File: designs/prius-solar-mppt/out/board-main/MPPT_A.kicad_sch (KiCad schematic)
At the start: 79 parts, among them J101 1757242, Q101 IAUC100N10, Q102 MMBTA42, Q103 IAUC100N10, Q104 IAUC100N10, Q105 IAUC100N10, Q106 IAUC100N10, U101 LM74700-Q1, U102 INA186A2QDBVRQ1, U103 LM5176QPWPRQ1, U104 TLV9001-Q1

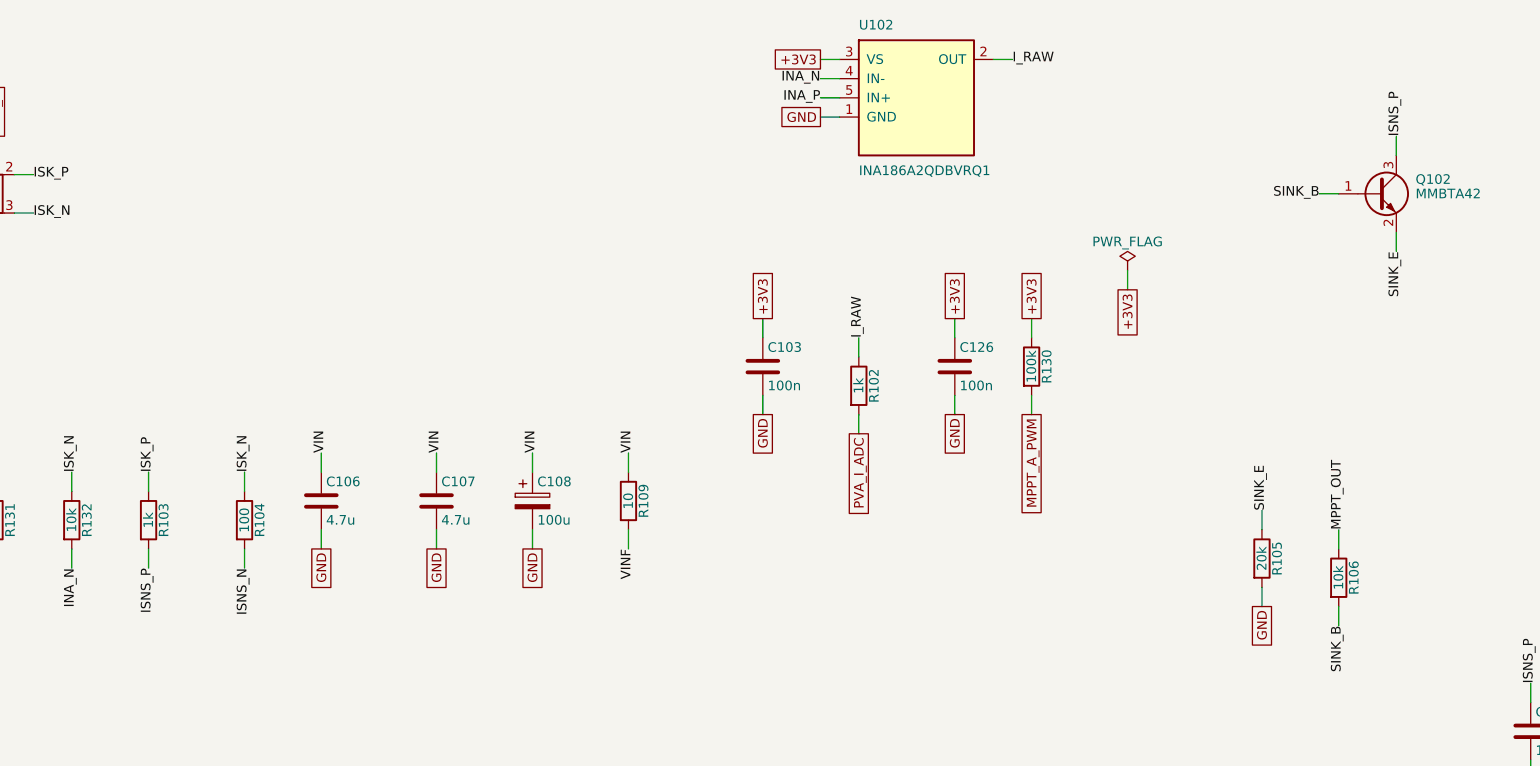
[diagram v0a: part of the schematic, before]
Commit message: designs/prius-solar-mppt: rework for the 2017 Prius Prime (Li-ion), charging car on and off
User decisions (2026-10-23): it is a Prius Prime with the Li-ion pack; it must charge
with the car on or off, be smart, and be weak enough that the pack cannot get into
trouble (stop by 80 %, voltage clamp, temperature compensation).

- Pack: 95 cells in series; no Prius pack is split while off (relays sit on the two pack
  cables; the service plug splits it only when pulled), so one tap pair on the cell side
  of the system main relays, fused on both poles, reaches the whole pack.
- Weak by construction: charge current capped at 0.30 A (>= 2 sun-days from 80 % to 100 %
  with firmware dead), analog CV/CC limiter on its own reference, latching overcurrent
  and overvoltage trips, 1:22 isolating DC transformer stage, 600 V relays, pack-sense
  core in the harness, event log, CAN transmit gated by ignition.
- Toyota's 180 W Prius PHV solar roof ("pump charging" through a buffer battery and the
  car's battery ECU) documented as the reference; this board does that ECU's job itself.
- Encoded in kaesynth: main (470 parts) and battery-end (15) boards, both netlists
  identical to the IR; 0 errors, 32 waived. The checks caught two v0.1 errors: an
  inverted UVLO (the stage never turned off) and the MPPT current sink on the wrong input.
- Blocking: roof measurement, junction-block tap location, installer/legality, roof
  fixing, and Q-10.

Co-Authored-By: Claude Opus 5.5 <noreply@anthropic.com>
Claude-Session: https://claude.ai/code/session_01VFJn9VbX8h27kf4LpLwEtn
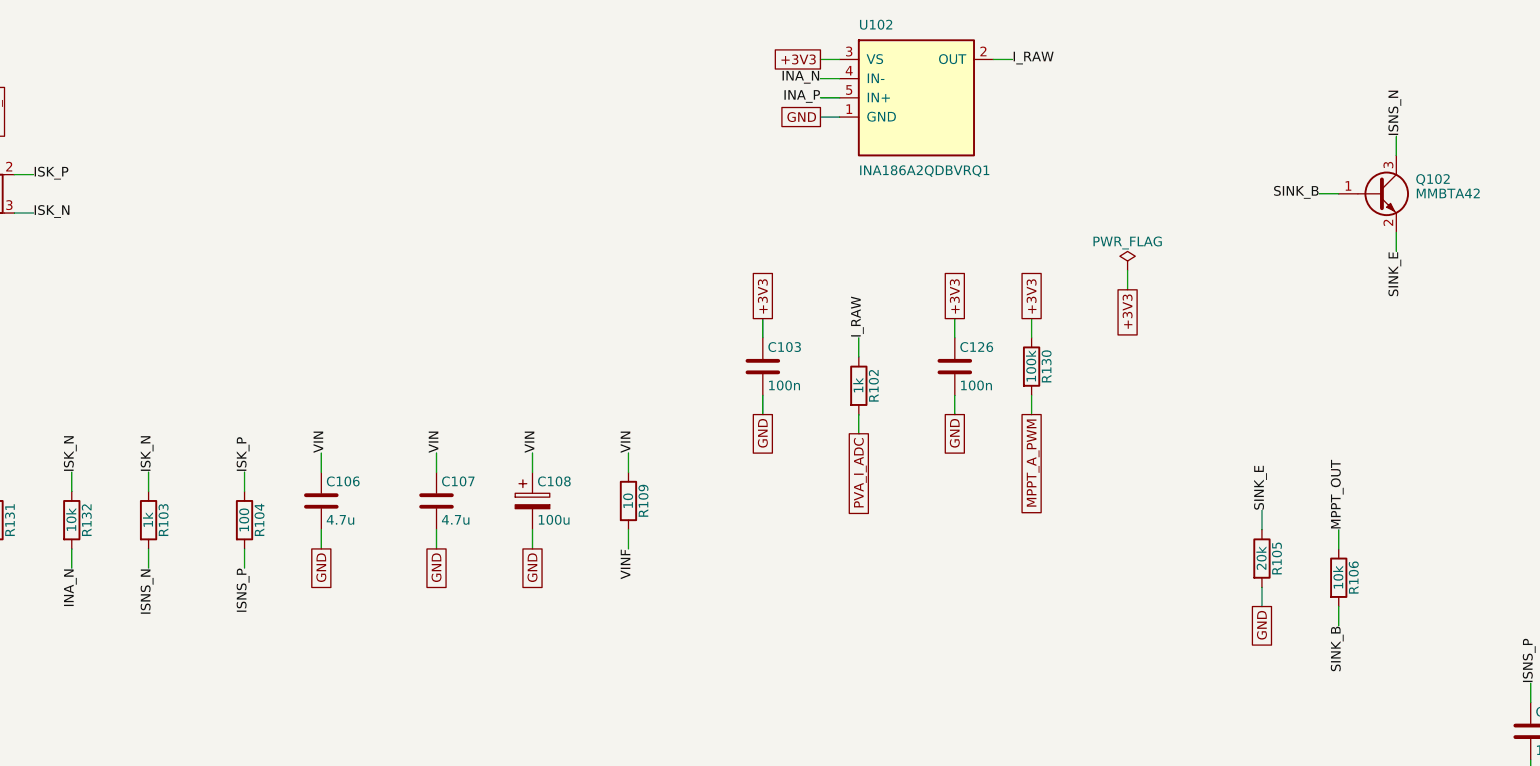
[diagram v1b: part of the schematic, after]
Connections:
- net ISK_N: now also R103.1; no longer R104.1
- net ISK_P: now also R104.1; no longer R103.1
- net ISNS_N: now also Q102.3 (C), R103.2; no longer R104.2
- net ISNS_P: now also R104.2; no longer Q102.3 (C), R103.2
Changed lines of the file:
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@@
 		)
 	)
-	(label "ISK_P"
+	(label "ISK_N"
 		(at 180.34 85.09 90)
 		(fields_autoplaced yes)
@@
 		)
 	)
-	(label "ISNS_P"
+	(label "ISNS_N"
 		(at 180.34 97.79 270)
 		(fields_autoplaced yes)
@@
 		)
 	)
-	(label "ISK_N"
+	(label "ISK_P"
 		(at 193.04 85.09 90)
 		(fields_autoplaced yes)
@@
 		)
 	)
-	(label "ISNS_N"
+	(label "ISNS_P"
 		(at 193.04 97.79 270)
 		(fields_autoplaced yes)
@@
 		)
 	)
-	(label "ISNS_P"
+	(label "ISNS_N"
 		(at 345.44 40.64 90)
 		(fields_autoplaced yes)

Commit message: designs/prius-solar-mppt: v0.3, fix the independent review's blockers and majors
- B1: CHASSIS domain with reinforced DC barriers to HV and PACK (10/8 mm), HV/PACK edge
  clearance 10 mm, mounting holes fixed with 13 mm keep-outs; thermal pedestal under LV
  parts only.
- B2: no primary source for the Prime's full-charge cell voltage was found (blocking
  Q-13); hardware clamp set below a 4.00 V/cell floor (L3 3.927 V, worst 3.963 V; L2
  3.836 V; L1 3.79 V) with DNP trim to raise later; until then charging may stop near
  55-65 % SOC.
- Majors: sink clamp + burst disable + PV-node trip and TVS against LM5176 reverse power;
  20 MHz AEC-Q200 crystal for CAN (listen-only start); parked insulation monitoring via a
  110 M bridge (also detects a welded relay); open-sensor-safe hardware OT; CAGE CLAMP HV
  terminals with a lid-switch HVIL; DCX on-time and 17.6 A primary overcurrent latches;
  supercap-held latch that clears overnight.
- Build: 0 errors, ERC clean, system and both board netlists identical; 9 waivers (17
  findings, was 32).

Co-Authored-By: Claude Opus 5.5 <noreply@anthropic.com>
Claude-Session: https://claude.ai/code/session_01VFJn9VbX8h27kf4LpLwEtn
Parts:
- added C130: 10n, Capacitor_SMD:C_0603_1608Metric, symbol Device:C
- added D106, D108: BAT46WJ, Diode_SMD:D_SOD-323F, symbol Diode:BAT46
- added D107: TPSMB43A, Diode_SMD:D_SMB, symbol Device:D_Zener
- added R133: 160k, Resistor_SMD:R_0603_1608Metric, symbol Device:R
- added R134: 10k, Resistor_SMD:R_0603_1608Metric, symbol Device:R
- R105: value 20k -> 75k; MPN ERJ-3EKF2002V -> ERJ-3EKF7502V
- R108: value 137k -> 162k; MPN ERJ-3EKF1373V -> ERJ-3EKF1623V
- R114: value 442k -> 432k; MPN TNPW1206442KBEEA -> TNPW1206432KBEEA
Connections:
- net EN: now also D106.2 (A), D108.2 (A)
- net GND: now also C130.2, D107.2 (A), R134.2
- net PVA_P: now also D107.1 (K), R133.1
- new net BURST_N: D106.1 (K)
- new net PVA_OVS: C130.1, R133.2, R134.1
- new net PVA_OV_N: D108.1 (K)
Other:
- moved on the sheet: C103, C104, C105, C106, C107, C108, C109, C110, C111, C112, C113, C114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
